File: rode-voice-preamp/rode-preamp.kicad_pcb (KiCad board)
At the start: 2 copper layers, 85 x 45 mm, 20 parts, among them J1 MIC IN, J2 TO UNO, U1 LM358

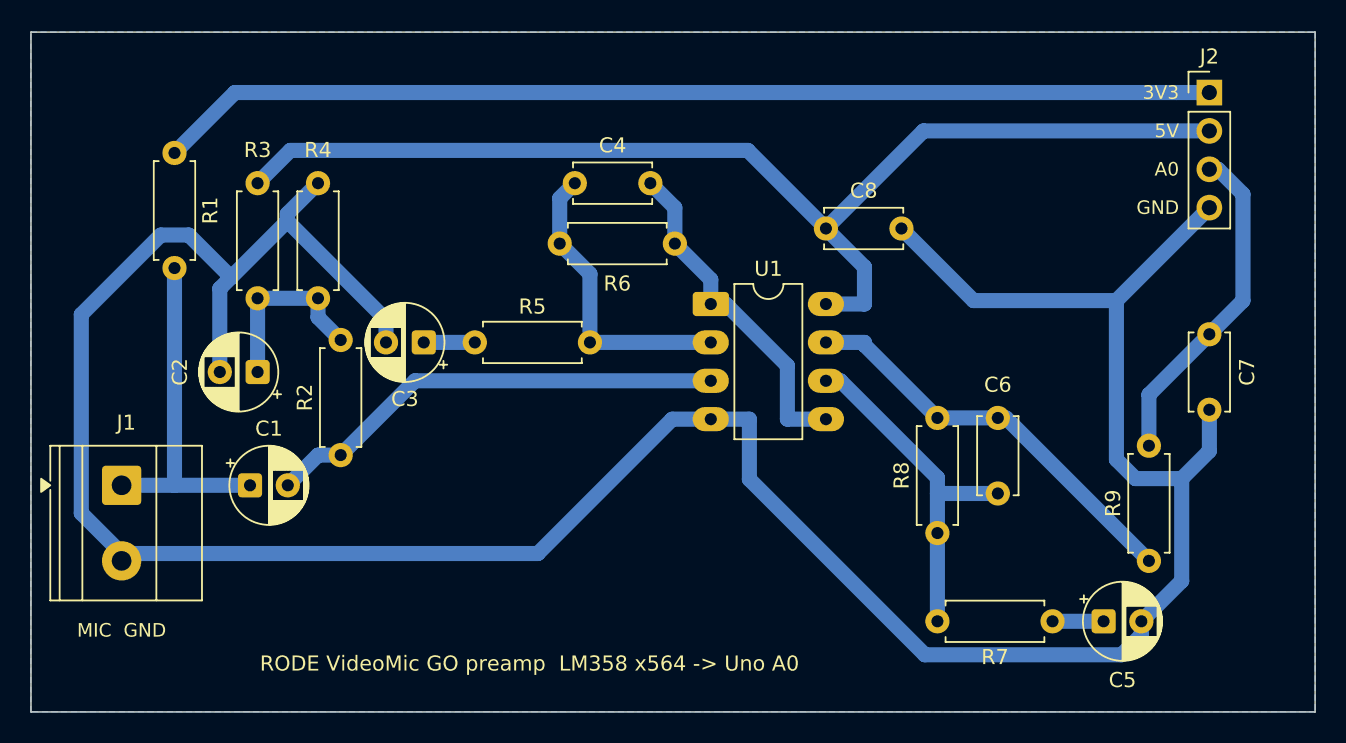
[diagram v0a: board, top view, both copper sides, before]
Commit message: RØDE preamp: shrink the board to 63 x 41 mm, solid pad connections
Stage A's feedback network moves above the LM358 and stage B packs to its
right, so the board drops from 85 x 45 to 63 x 41 mm with the same
topology: rails along the top edge, OUT_A under the package, single-sided
with 0 vias and 0 wire bridges. The GND pour now connects its pads solid
instead of through thermal spokes. DRC and schematic parity are clean;
production files and renders are regenerated.
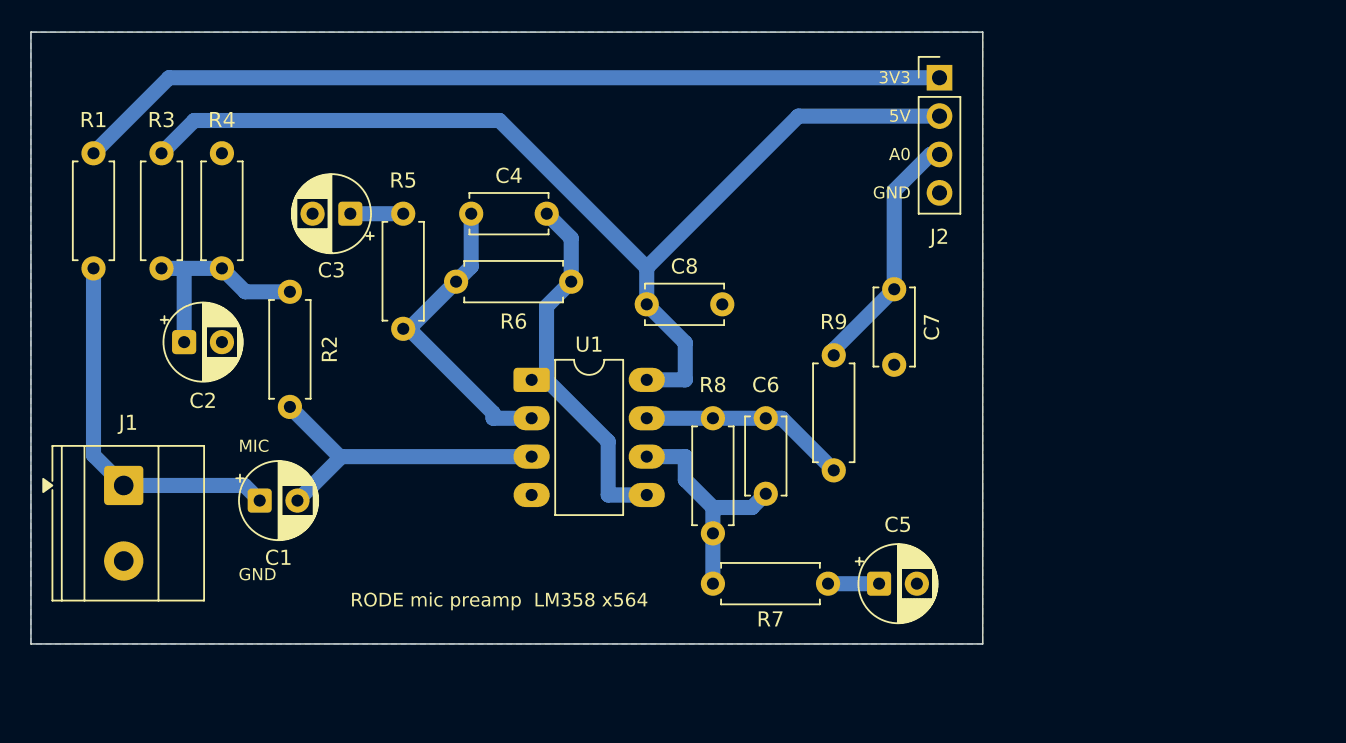
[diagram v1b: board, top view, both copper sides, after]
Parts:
- moved R9 21.7 mm to (153.1, 129.0)
- moved C7 21.1 mm to (157.1, 117.0)
- moved J2 17.9 mm to (160.1, 103.0)
- moved C6 15.4 mm to (148.6, 130.6)
- moved C5 15.1 mm to (156.1, 136.5)
- moved R7 15.1 mm to (152.8, 136.5)
- moved R8 14.9 mm to (145.1, 133.2)
- moved C8 12.9 mm to (140.8, 118.0)
- moved U1 12.9 mm to (133.1, 123.0)
- moved C3 9.81 mm to (121.1, 112.0)
- moved R5 9.75 mm to (124.6, 112.0), turned to -90 degrees
- moved R6 7.31 mm to (128.1, 116.5)
- moved C4 7.15 mm to (129.1, 112.0)
- moved R3 6.66 mm to (108.6, 108.0)
- moved R4 6.66 mm to (112.6, 115.6)
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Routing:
- net GND: track 194.2 -> 0.00 mm
- net /OUT_B: track 27.5 -> 13.8 mm
- net +3V3: track 70.2 -> 58.1 mm
- net Net-(U1A-+): track 30.9 -> 21.4 mm
- net Net-(U1B--): track 23.5 -> 15.6 mm
- net +5V: track 77.3 -> 71.6 mm
- net /A0: track 22.1 -> 16.5 mm
- net /OUT_A: track 22.5 -> 25.2 mm
- net /BIAS: track 12.3 -> 14.0 mm
- net /MIC: track 22.9 -> 24.6 mm
- net Net-(U1A--): track 19.8 -> 20.5 mm
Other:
- board size 85 x 45 mm -> 63 x 40.5 mm
- board text added: "MIC"
- board text added: "RODE mic preamp LM358 x564"
- board text removed: "MIC GND"
- board text removed: "RODE VideoMic GO preamp LM358 x564 -> Uno A0"

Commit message: final rode pcb layout
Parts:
- moved U1 11.2 mm to (122.5, 126.5)
- moved C5 10.6 mm to (145.5, 136.5)
- moved C6 10.6 mm to (138.0, 130.5)
- moved C7 10.6 mm to (146.5, 117.0)
- moved J2 10.6 mm to (149.5, 103.0)
- moved R7 10.6 mm to (142.2, 136.5)
- moved R8 10.6 mm to (134.5, 133.1)
- moved R9 10.6 mm to (142.5, 129.0)
- moved C8 8.36 mm to (133.7, 122.5)
- moved C1 0.39 mm to (115.1, 131.4)
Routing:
- net +3V3: track 58.1 -> 47.5 mm
- net /OUT_A: track 25.2 -> 35.2 mm
- net Net-(U1A-+): track 21.4 -> 11.7 mm
- net /A0: track 16.5 -> 19.6 mm
- net Net-(U1A--): track 20.5 -> 23.4 mm
- net Net-(U1B--): track 15.6 -> 13.4 mm
- net /OUT_B: track 13.8 -> 15.3 mm
- net +5V: track 71.6 -> 73.0 mm
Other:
- board size 63 x 40.5 mm -> 53.4 x 40.5 mm
